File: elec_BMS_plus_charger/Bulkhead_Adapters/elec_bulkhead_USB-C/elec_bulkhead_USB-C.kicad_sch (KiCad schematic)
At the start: 10 parts

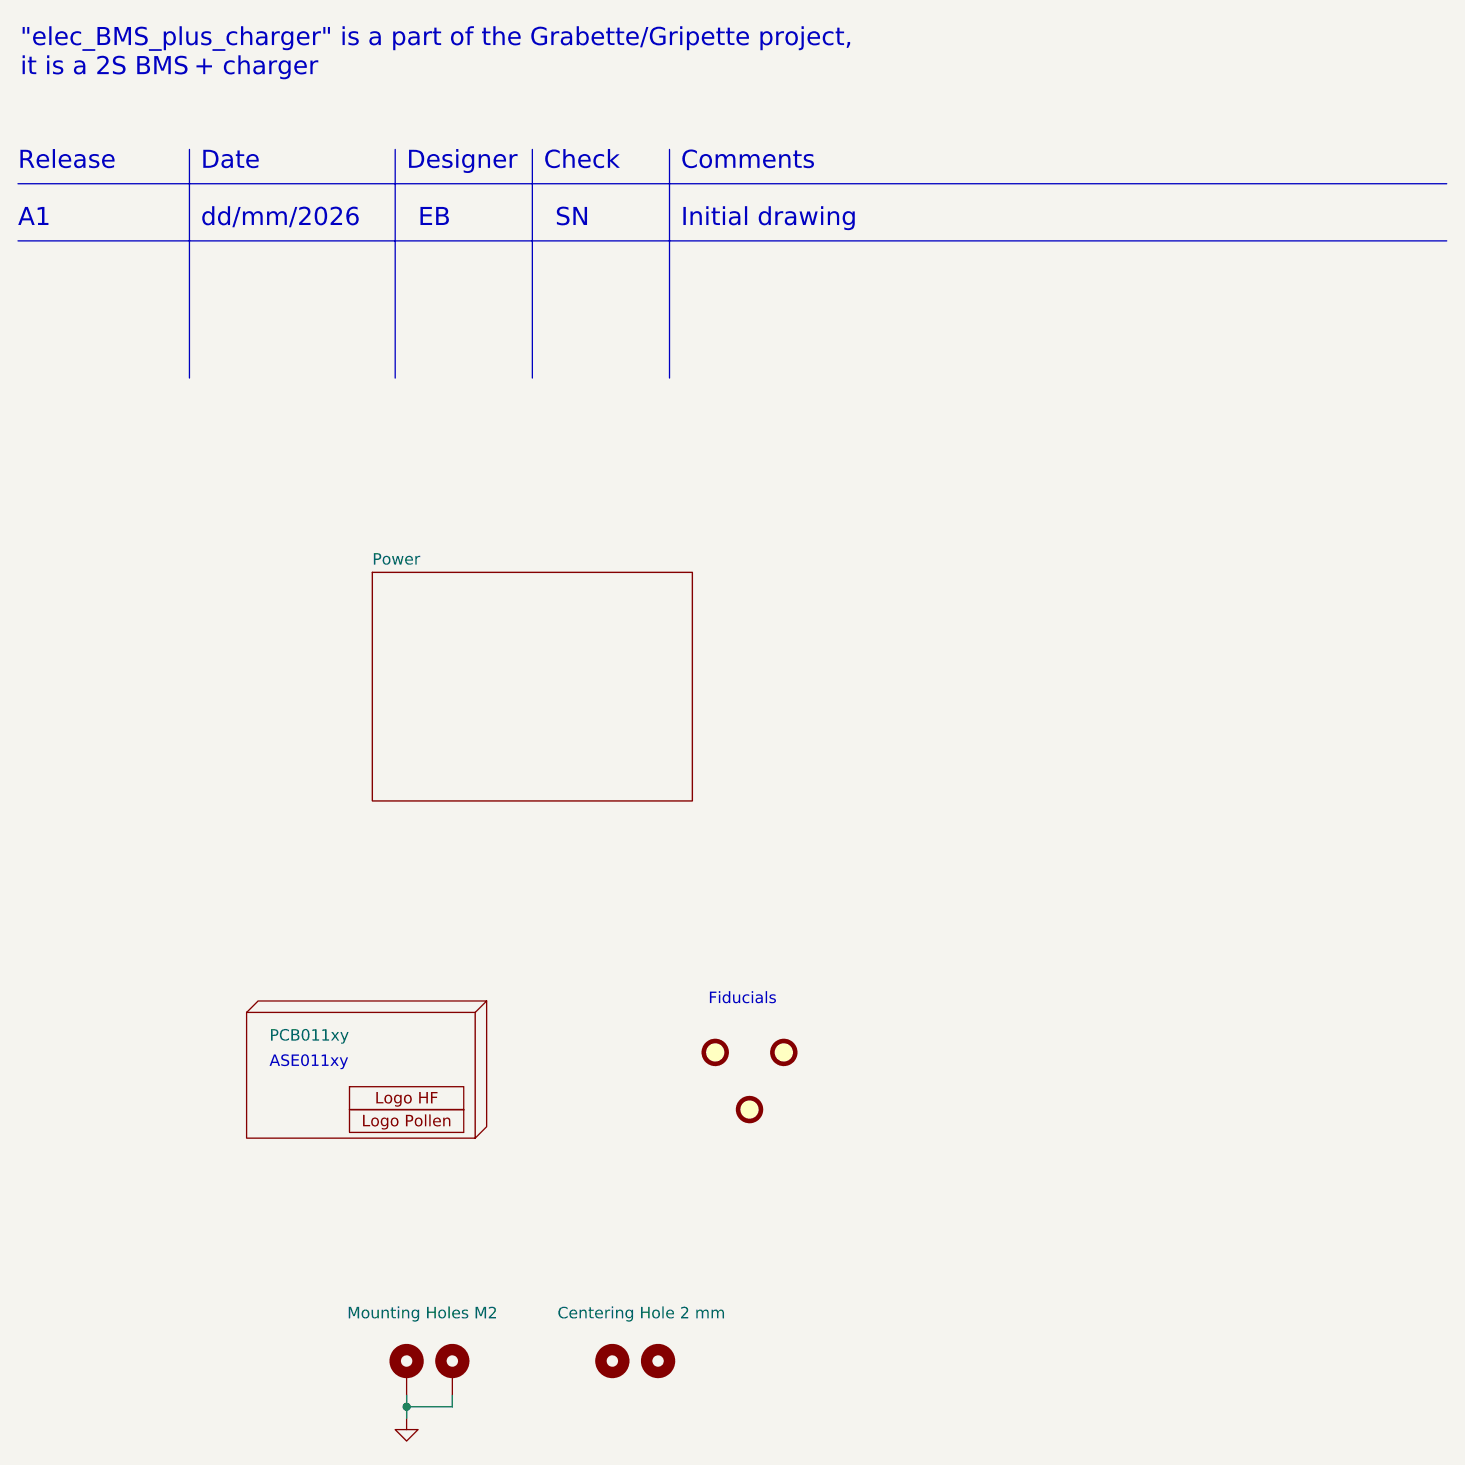
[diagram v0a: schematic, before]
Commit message: [update] BMS schematic DRC 0k.
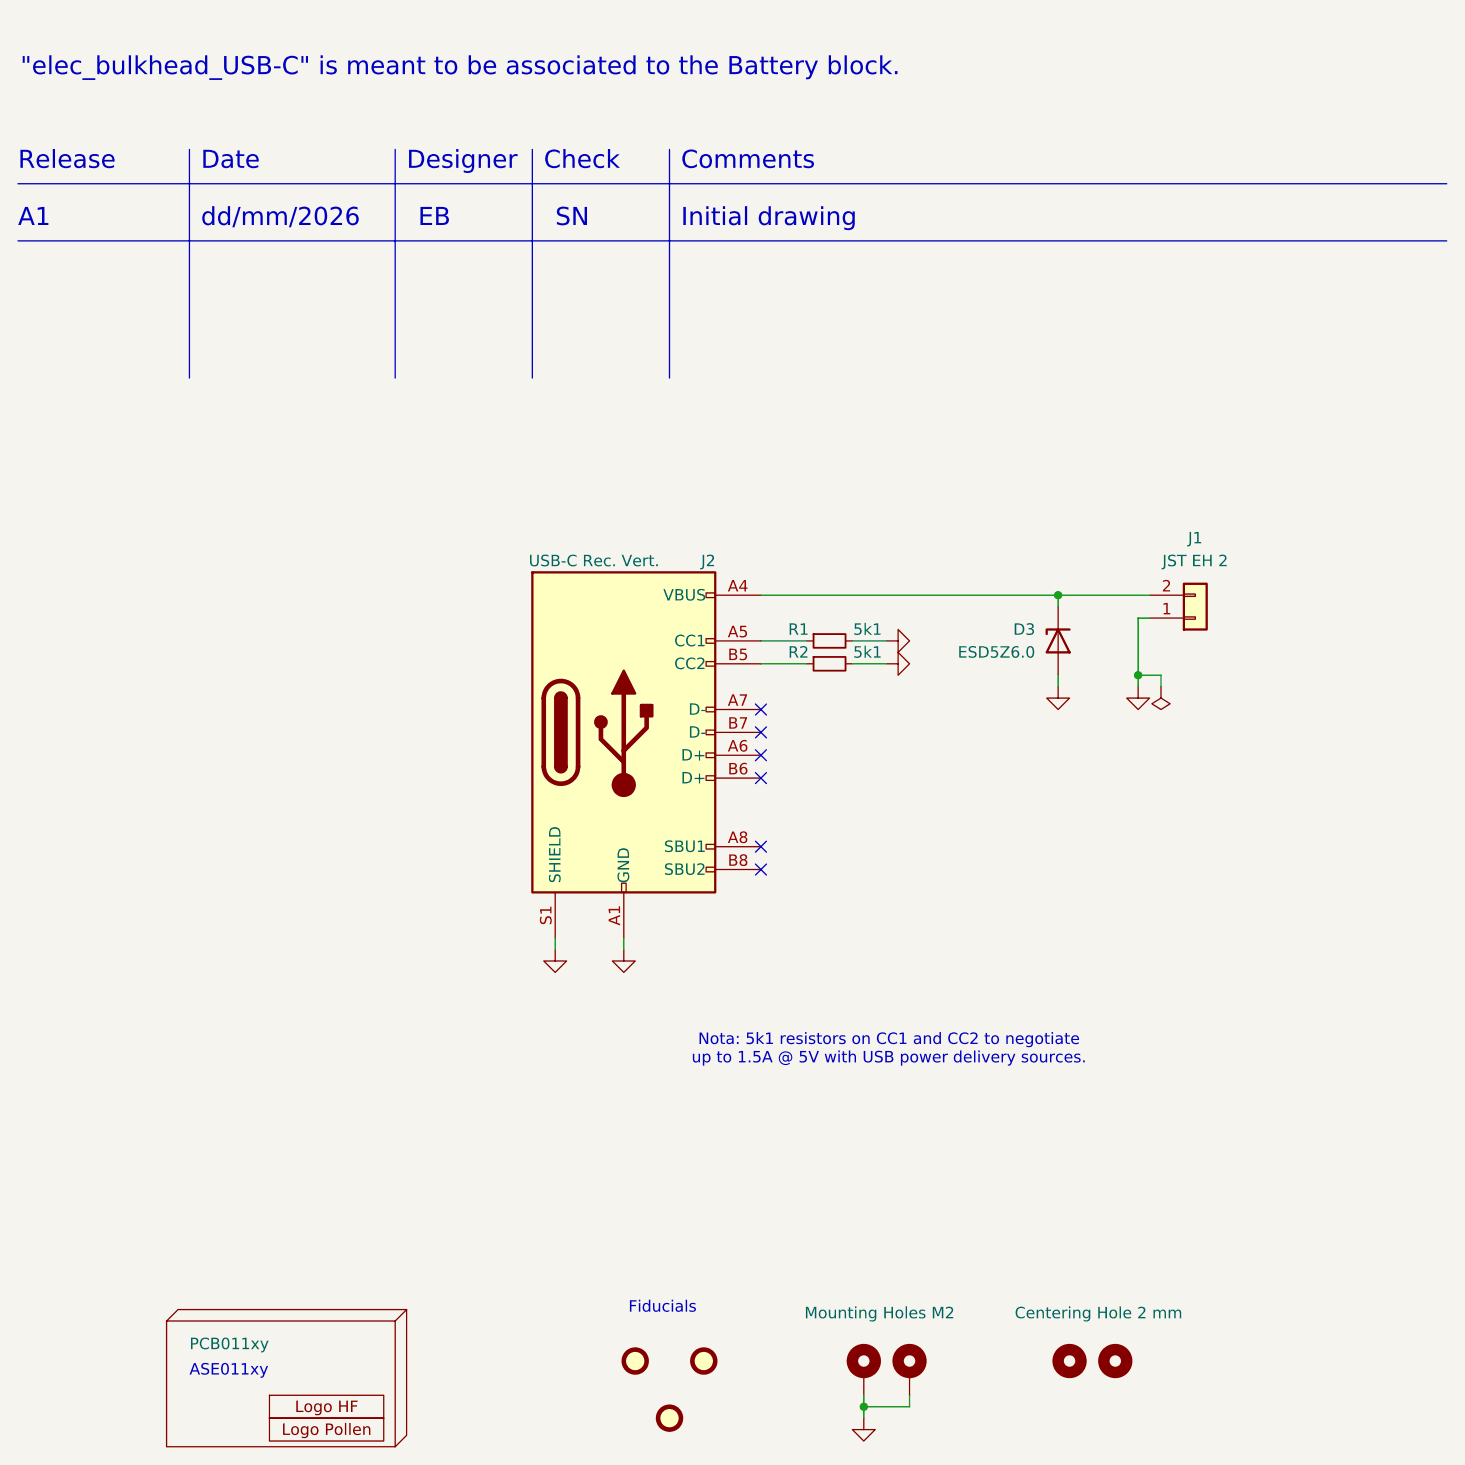
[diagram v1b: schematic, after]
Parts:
- added D3: ESD5Z6.0, Diode_SMD:D_SOD-523, symbol Diode:ESD5Zxx
- added J1: JST EH 2, Connector_JST:JST_EH_B2B-EH-A_1x02_P2.50mm_Vertical, symbol Connector_Generic:Conn_01x02
- added J2: USB-C Rec. Vert., Library_Pollen:USB-C_16p_vert_Shou-Han_TYPE-C 16P LTH6.8 - C5187468, symbol Connector:USB_C_Receptacle_USB2.0_16P
- added R1, R2: 5k1, Resistor_SMD:R_0402_1005Metric, symbol Device:R_Small
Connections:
- net GND: now also D3.2 (A), J1.1 (Pin_1), J2.A1 (GND), J2.A12 (GND), J2.B1 (GND), J2.B12 (GND), J2.S1 (SHIELD), R1.2, R2.2
- new net: D3.1 (K), J1.2 (Pin_2), J2.A4 (VBUS), J2.A9 (VBUS), J2.B4 (VBUS), J2.B9 (VBUS)
- new net: J2.B5 (CC2), R2.1
- new net: J2.A5 (CC1), R1.1
- no-connect marks 0 -> 6
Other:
- removed sheet Power
- note added: ""elec_bulkhead_USB-C" is meant to be associated to the Battery block."
- note added: "Nota: 5k1 resistors on CC1 and CC2 to negotiate up to 1.5A @ 5V with USB power delivery sources."
- note removed: ""elec_BMS_plus_charger" is a part of the Grabette/Gripette project, it is a 2S BMS + charger"
- title: Grabette - BMS + charger -> Grabette - USB-C Bulkhead for Battery Bloc
